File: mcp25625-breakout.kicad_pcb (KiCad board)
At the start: 2 copper layers, 25.4 x 14 mm, 7 parts, among them J1 Conn_01x10, SW1 SW_Slide_with_cover, U1 MCP25625-x-SS, Y1 Resonator

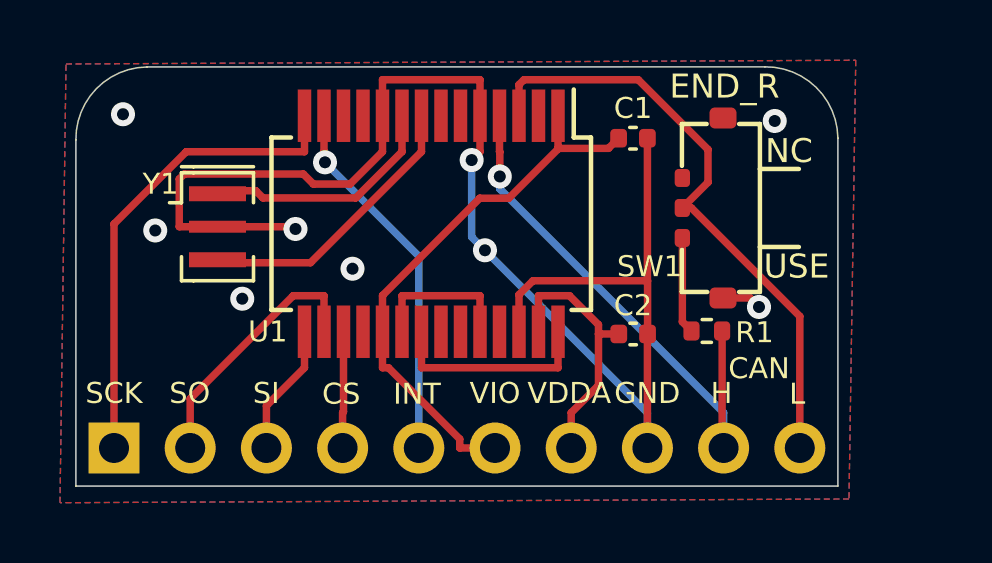
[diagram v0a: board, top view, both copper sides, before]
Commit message: Add reset pad and 16MHz mems as rev2021.07
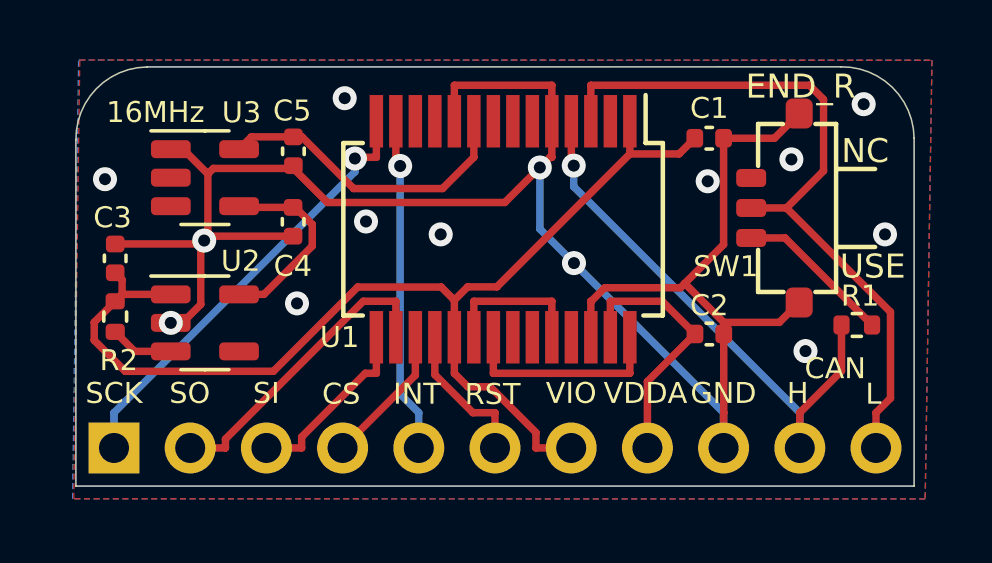
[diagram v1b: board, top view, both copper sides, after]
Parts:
- removed Y1: Resonator, my-kicad-footprints:Resonator_SMD_Murata_CSTxExxV-3Pin_3.0x1.1mm_narrow
- added C3: 0.1uf, Capacitor_SMD:C_0402_1005Metric, F.Cu at (138.0, 77.7)
- added C4: 1uf, Capacitor_SMD:C_0402_1005Metric, F.Cu at (144.0, 76.5)
- added C5: 22pf, Capacitor_SMD:C_0402_1005Metric, F.Cu at (144.0, 74.1)
- added R2: 10k, Resistor_SMD:R_0402_1005Metric, F.Cu at (138.0, 79.6)
- added U2: NJM2866F33, Package_TO_SOT_SMD:SOT-23-5, F.Cu at (141.0, 79.8)
- added U3: SiT2001B-MEMS-Clock-Generator, Package_TO_SOT_SMD:SOT-23-5, F.Cu at (141.0, 75.0)
- J1: value Conn_01x10 -> Conn_01x11; footprint my-kicad-footprints:PinHeader_1x10_P2.54mm_Vertical_witout_silk -> my-kicad-footprints:PinHeader_1x11_P2.54mm_Vertical_witout_silk
- moved R1 5.00 mm to (162.8, 79.9), turned to 0 degrees
- moved C1 2.54 mm to (157.8, 73.7)
- moved C2 2.54 mm to (157.8, 80.2)
- moved SW1 2.54 mm to (160.8, 76.0)
- moved U1 2.40 mm to (151.0, 76.7)
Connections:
- J1 pad 10: /CANL -> /CANH
- J1 pad 6: /V_IO -> /RESET
- J1 pad 7: /V_DDA -> /V_IO
- J1 pad 8: GND -> /V_DDA
- J1 pad 9: /CANH -> GND
- U1 pad 18: Net-(U1-Pad18) -> /RESET
- U1 pad 9: Net-(U1-Pad9) -> /16MHz
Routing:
- net /V_IO: track 18.6 -> 37.1 mm
- net GND: track 50.8 -> 66.1 mm, vias 9 -> 14
- net /16MHz: track 0.00 -> 10.3 mm
- net Net-(U1-Pad8): track 9.53 -> 0.00 mm
- net Net-(U1-Pad9): track 8.09 -> 0.00 mm
- net +3V3: track 0.00 -> 6.52 mm
- net /RESET: track 0.00 -> 4.95 mm
- net /CANL: track 20.5 -> 24.1 mm
- net Net-(R2-Pad2): track 0.00 -> 2.12 mm
- net Net-(R1-Pad2): track 3.23 -> 5.23 mm
- net /SI: track 4.40 -> 6.11 mm
- net /SO: track 8.72 -> 10.3 mm
- net /INT: track 12.4 -> 11.2 mm
- net /SCK: track 16.0 -> 14.9 mm, vias 0 -> 1
- net /CS: track 3.89 -> 4.69 mm
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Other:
- board size 25.4 x 14 mm -> 27.9 x 14 mm
- board text added: "16MHz"
- board text added: "RST"
- board text added: "Reset"
- board text added: "Rev2021.07"
- board text removed: "Rev2021.06"

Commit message: Replace rezonator to crystal
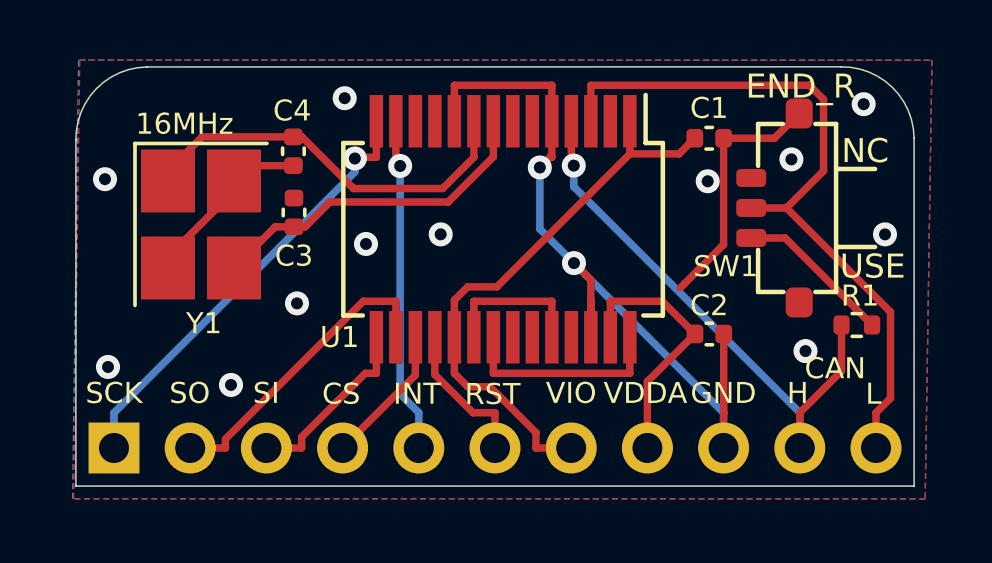
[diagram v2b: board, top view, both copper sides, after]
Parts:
- removed the C4 at (144.0, 76.5)
- removed R2: 10k, Resistor_SMD:R_0402_1005Metric
- removed U2: NJM2866F33, Package_TO_SOT_SMD:SOT-23-5
- removed U3: SiT2001B-MEMS-Clock-Generator, Package_TO_SOT_SMD:SOT-23-5
- added Y1: Crystal_GND24_16MHz, Crystal:Crystal_SMD_SeikoEpson_FA238-4Pin_3.2x2.5mm_HandSoldering, F.Cu at (140.9, 76.5)
- C3: value 0.1uf -> 22pf
- moved C3 6.15 mm to (144.0, 76.2)
- renumbered C5 to C4
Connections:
- net /16MHz renamed Net-(C4-Pad1)
- C3 pad 1: /V_IO -> Net-(C3-Pad1)
- U1 pad 8: Net-(U1-Pad8) -> Net-(C3-Pad1)
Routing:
- net GND: track 66.1 -> 41.4 mm
- net /V_IO: track 37.1 -> 19.0 mm
- net Net-(C3-Pad1): track 0.00 -> 11.4 mm
- net +3V3: track 6.52 -> 0.00 mm
- net Net-(C4-Pad1): track 10.3 -> 13.3 mm
- net Net-(R2-Pad2): track 2.12 -> 0.00 mm
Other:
- board text added: "Rev2021.10"
- board text removed: "Rev2021.07"

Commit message: Apply KiCad6
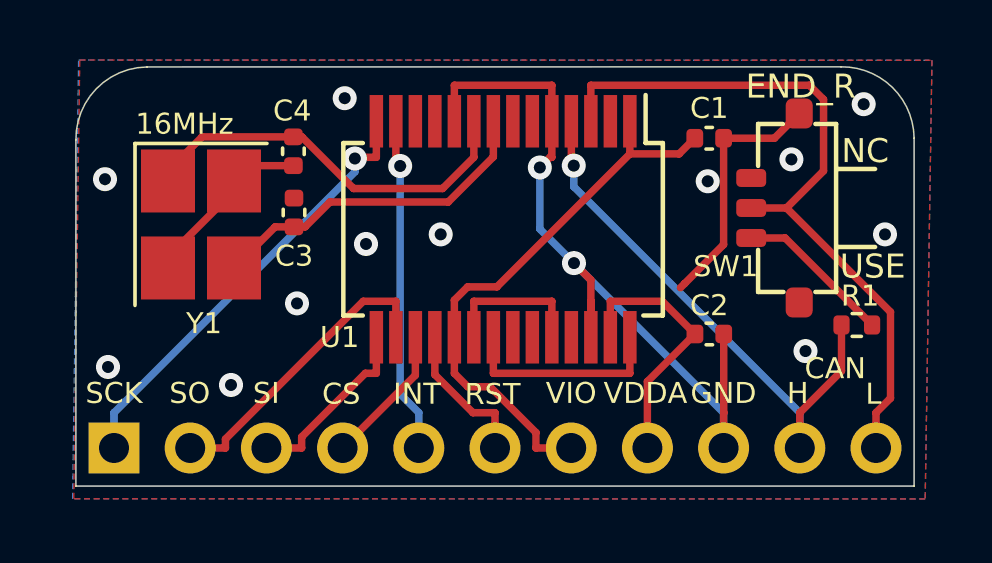
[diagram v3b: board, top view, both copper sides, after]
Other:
- net class Default removed

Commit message: Apply KiCad6 lib
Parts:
- J1: footprint my-kicad-footprints:PinHeader_1x11_P2.54mm_Vertical_witout_silk -> asukiaaa-kicad-footprints:PinHeader_1x11_P2.54mm_Vertical_witout_silk
- SW1: footprint my-kicad-footprints:slide_switch_smd -> asukiaaa-kicad-footprints:slide_switch_smd
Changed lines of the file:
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@@
     )
   )
-  (footprint "my-kicad-footprints:PinHeader_1x11_P2.54mm_Vertical_witout_silk" (layer "F.Cu")
+  (footprint "asukiaaa-kicad-footprints:PinHeader_1x11_P2.54mm_Vertical_witout_silk" (layer "F.Cu")
     (at 138 84 90)
     (descr "Through hole straight pin header, 1x08, 2.54mm pitch, single row")
@@
     )
   )
-  (footprint "my-kicad-footprints:slide_switch_smd" (layer "F.Cu")
+  (footprint "asukiaaa-kicad-footprints:slide_switch_smd" (layer "F.Cu")
     (at 160.84 76 90)
     (descr "https://akizukidenshi.com/download/ds/alps/ssaj120100.pdf")

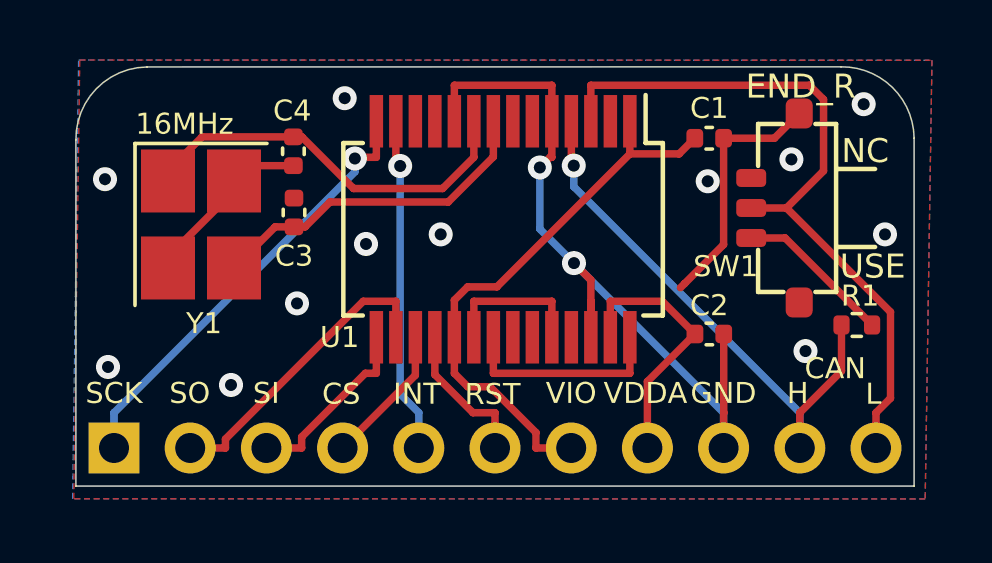
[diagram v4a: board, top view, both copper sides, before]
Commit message: Change to not hand solder pad for crystal
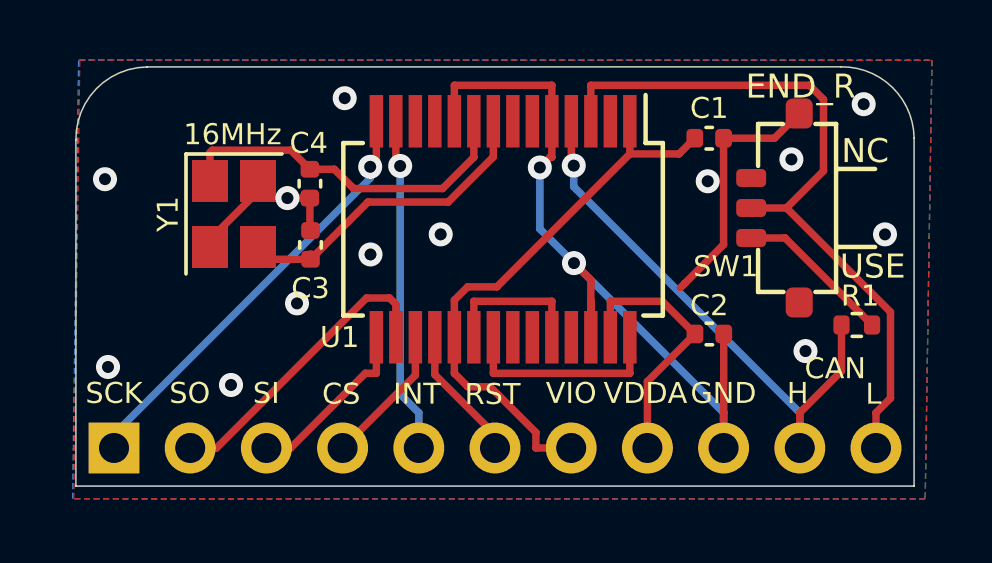
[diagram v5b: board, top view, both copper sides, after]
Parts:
- Y1: footprint Crystal:Crystal_SMD_SeikoEpson_FA238-4Pin_3.2x2.5mm_HandSoldering -> Crystal:Crystal_SMD_SeikoEpson_FA238-4Pin_3.2x2.5mm
- moved C3 1.21 mm to (144.6, 77.2)
- moved C4 1.21 mm to (144.5, 75.2)
- moved Y1 1.15 mm to (142.0, 76.2)
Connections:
- SW1 pad 3: Net-(SW1-Pad3) -> unconnected-(SW1-Pad3)
- U1 pad 11: Net-(U1-Pad11) -> unconnected-(U1-Pad11)
- U1 pad 12: Net-(U1-Pad12) -> unconnected-(U1-Pad12)
- U1 pad 2: Net-(U1-Pad2) -> unconnected-(U1-Pad2)
- U1 pad 22: Net-(U1-Pad22) -> unconnected-(U1-Pad22)
- U1 pad 23: Net-(U1-Pad23) -> unconnected-(U1-Pad23)
- U1 pad 25: Net-(U1-Pad25) -> unconnected-(U1-Pad25)
- U1 pad 6: Net-(U1-Pad6) -> unconnected-(U1-Pad6)
- U1 pad 7: Net-(U1-Pad7) -> unconnected-(U1-Pad7)
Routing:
- net Net-(C4-Pad1): track 13.3 -> 11.9 mm
- net Net-(C3-Pad1): track 11.4 -> 10.6 mm
- net GND: vias 14 -> 15
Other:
- board text added: "Rev2023.02"
- board text removed: "Rev2021.10"

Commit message: Add resistor between rst and vio as rev2023.05
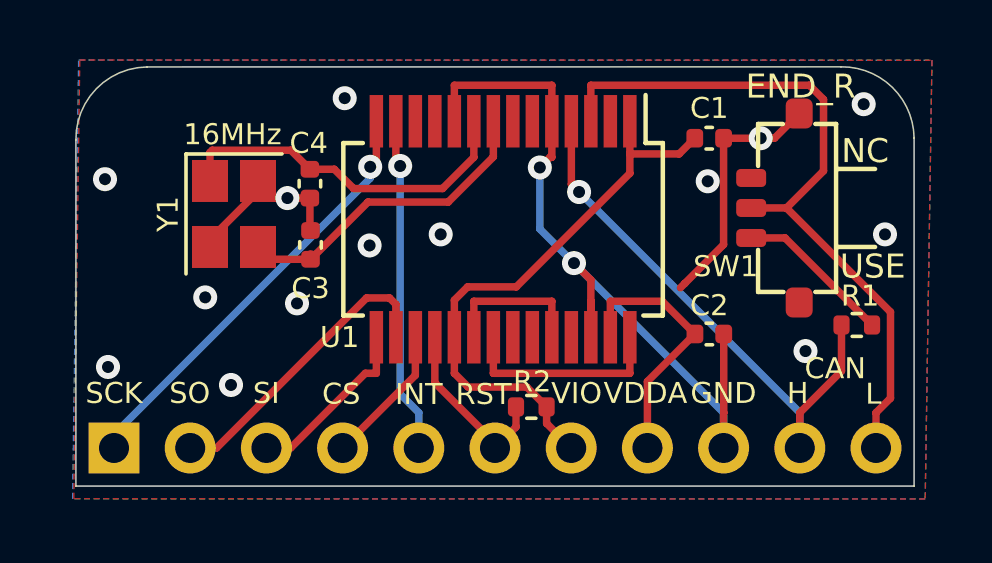
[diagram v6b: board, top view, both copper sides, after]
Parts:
- added R2: 10k, Resistor_SMD:R_0402_1005Metric, F.Cu at (151.9, 82.6)
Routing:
- net /RESET: track 4.52 -> 6.18 mm
- net GND: vias 15 -> 16
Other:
- board text added: "Rev2023.05"
- board text removed: "Rev2023.02"
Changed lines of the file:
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@@
+    )
+  )
+  (footprint "Resistor_SMD:R_0402_1005Metric" (layer "F.Cu")
+    (at 151.91 82.63 180)
+    (descr "Resistor SMD 0402 (1005 Metric), square (rectangular) end terminal, IPC_7351 nominal, (Body size source: IPC-SM-782 page 72, https://www.pcb-3d.com/wordpress/wp-content/uploads/ipc-sm-782a_amendment_1_and_2.pdf), generated with kicad-footprint-generator")
+    (tags "resistor")
+    (property "Sheetfile" "mcp25625-breakout.kicad_sch")
+    (property "Sheetname" "")
+    (attr smd)
+    (fp_text reference "R2" (at -0.03 0.84) (layer "F.SilkS")
+      (effects (font (size 0.7 0.7) (thickness 0.15)))
+    )
+    (fp_text value "10k" (at 0 1.17) (layer "F.Fab")
+      (effects (font (size 1 1) (thickness 0.15)))
+    )
+    (fp_text user "${REFERENCE}" (at 0 0) (layer "F.Fab")
+      (effects (font (size 0.26 0.26) (thickness 0.04)))
+    )
+    (fp_line (start -0.153641 -0.38) (end 0.153641 -0.38) (layer "F.SilkS") (width 0.12))
+    (fp_line (start -0.153641 0.38) (end 0.153641 0.38) (layer "F.SilkS") (width 0.12))
+    (fp_line (start 0.93 0.47) (end -0.93 0.47) (layer "F.CrtYd") (width 0.05))
+    (fp_line (start -0.93 0.47) (end -0.93 -0.47) (layer "F.CrtYd") (width 0.05))
+    (fp_line (start -0.93 -0.47) (end 0.93 -0.47) (layer "F.CrtYd") (width 0.05))
+    (fp_line (start 0.93 -0.47) (end 0.93 0.47) (layer "F.CrtYd") (width 0.05))
+    (fp_line (start 0.525 0.27) (end -0.525 0.27) (layer "F.Fab") (width 0.1))
+    (fp_line (start 0.525 -0.27) (end 0.525 0.27) (layer "F.Fab") (width 0.1))
+    (fp_line (start -0.525 -0.27) (end 0.525 -0.27) (layer "F.Fab") (width 0.1))
+    (fp_line (start -0.525 0.27) (end -0.525 -0.27) (layer "F.Fab") (width 0.1))
+    (pad "1" smd roundrect (at -0.51 0 180) (size 0.54 0.64) (layers "F.Cu" "F.Paste" "F.Mask") (roundrect_rratio 0.25)
+      (net 2 "/V_IO") (pintype "passive"))
+    (pad "2" smd roundrect (at 0.51 0 180) (size 0.54 0.64) (layers "F.Cu" "F.Paste" "F.Mask") (roundrect_rratio 0.25)
+      (net 23 "/RESET") (pintype "passive"))
+    (model "${KICAD6_3DMODEL_DIR}/Resistor_SMD.3dshapes/R_0402_1005Metric.wrl"
+      (offset (xyz 0 0 0))
+      (scale (xyz 1 1 1))
+      (rotate (xyz 0 0 0))
     )
   )
@@
   (gr_line (start 164.67 85.27) (end 164.67 73.67) (layer "Edge.Cuts") (width 0.05))
   (gr_arc (start 136.73 73.73) (mid 137.411731 72.024157) (end 139.1 71.3) (layer "Edge.Cuts") (width 0.05))
-  (gr_text "Rev2023.02" (at 157.265 74.325) (layer "B.SilkS")
+  (gr_text "Rev2023.05" (at 157.265 74.325) (layer "B.SilkS")
     (effects (font (size 1 1) (thickness 0.15)) (justify mirror))
   )
@@
     (effects (font (size 0.8 0.8) (thickness 0.15)))
   )
-  (gr_text "RST" (at 150.62 82.21) (layer "F.SilkS")
+  (gr_text "RST" (at 150.32 82.21) (layer "F.SilkS")
     (effects (font (size 0.7 0.7) (thickness 0.13)))
   )
@@
     (effects (font (size 0.7 0.7) (thickness 0.13)))
   )
-  (gr_text "INT" (at 148.1 82.2) (layer "F.SilkS")
+  (gr_text "INT" (at 148.16 82.21) (layer "F.SilkS")
     (effects (font (size 0.7 0.7) (thickness 0.13)))
   )
@@
     (effects (font (size 0.7 0.7) (thickness 0.13)))
   )
-  (gr_text "VIO" (at 153.24 82.175) (layer "F.SilkS")
+  (gr_text "VIO" (at 153.42 82.18) (layer "F.SilkS")
     (effects (font (size 0.7 0.7) (thickness 0.13)))
   )
@@
   (via (at 137.8 81.3) (size 0.8) (drill 0.4) (layers "F.Cu" "B.Cu") (net 1))
   (via (at 161.05 80.77) (size 0.8) (drill 0.4) (layers "F.Cu" "B.Cu") (net 1))
-  (via (at 146.55 77.55) (size 0.8) (drill 0.4) (layers "F.Cu" "B.Cu") (net 1))
+  (via (at 146.52 77.25) (size 0.8) (drill 0.4) (layers "F.Cu" "B.Cu") (net 1))
   (via (at 152.1945 74.6505) (size 0.8) (drill 0.4) (layers "F.Cu" "B.Cu") (net 1))
-  (via (at 160.58 74.38) (size 0.8) (drill 0.4) (layers "F.Cu" "B.Cu") (net 1))
+  (via (at 141.04 78.98) (size 0.8) (drill 0.4) (layers "F.Cu" "B.Cu") (free) (net 1))
+  (via (at 159.555 73.675) (size 0.8) (drill 0.4) (layers "F.Cu" "B.Cu") (net 1))
   (via (at 137.7 75.04) (size 0.8) (drill 0.4) (layers "F.Cu" "B.Cu") (net 1))
   (segment (start 153.33265 77.83735) (end 152.1945 76.6992) (width 0.25) (layer "B.Cu") (net 1))
@@
   (segment (start 158.32 84) (end 158.32 82.8247) (width 0.25) (layer "B.Cu") (net 1))
   (segment (start 152.1945 76.6992) (end 152.1945 74.6505) (width 0.25) (layer "B.Cu") (net 1))
-  (segment (start 149.345 79.0724) (end 149.345 80.31) (width 0.25) (layer "F.Cu") (net 2))
+  (segment (start 149.345 79.0724) (end 149.7884 78.629) (width 0.25) (layer "F.Cu") (net 2))
+  (segment (start 149.8047 81.97) (end 151.76 81.97) (width 0.25) (layer "F.Cu") (net 2))
+  (segment (start 149.7884 78.629) (end 151.411 78.629) (width 0.25) (layer "F.Cu") (net 2))
   (segment (start 156.8371 74.1979) (end 155.195 74.1979) (width 0.25) (layer "F.Cu") (net 2))
   (segment (start 157.36 73.675) (end 156.8371 74.1979) (width 0.25) (layer "F.Cu") (net 2))
-  (segment (start 149.345 81.5103) (end 149.7954 81.9607) (width 0.25) (layer "F.Cu") (net 2))
-  (segment (start 149.7884 78.629) (end 150.7639 78.629) (width 0.25) (layer "F.Cu") (net 2))
-  (segment (start 149.7954 81.9607) (end 150.5396 81.9607) (width 0.25) (layer "F.Cu") (net 2))
-  (segment (start 152.0647 83.4858) (end 152.0647 84) (width 0.25) (layer "F.Cu") (net 2))
-  (segment (start 153.24 84) (end 152.0647 84) (width 0.25) (layer "F.Cu") (net 2))
+  (segment (start 155.195 74.845) (end 155.195 74.1979) (width 0.25) (layer "F.Cu") (net 2))
+  (segment (start 152.42 83.18) (end 153.24 84) (width 0.25) (layer "F.Cu") (net 2))
+  (segment (start 151.411 78.629) (end 155.195 74.845) (width 0.25) (layer "F.Cu") (net 2))
   (segment (start 149.345 80.31) (end 149.345 81.5103) (width 0.25) (layer "F.Cu") (net 2))
-  (segment (start 150.5396 81.9607) (end 152.0647 83.4858) (width 0.25) (layer "F.Cu") (net 2))
   (segment (start 155.195 73.11) (end 155.195 74.1979) (width 0.25) (layer "F.Cu") (net 2))
-  (segment (start 150.7639 78.629) (end 155.195 74.1979) (width 0.25) (layer "F.Cu") (net 2))
-  (segment (start 149.345 79.0724) (end 149.7884 78.629) (width 0.25) (layer "F.Cu") (net 2))
+  (segment (start 149.345 80.31) (end 149.345 79.0724) (width 0.25) (layer "F.Cu") (net 2))
+  (segment (start 151.76 81.97) (end 152.42 82.63) (width 0.25) (layer "F.Cu") (net 2))
+  (segment (start 149.345 81.5103) (end 149.8047 81.97) (width 0.25) (layer "F.Cu") (net 2))
+  (segment (start 152.42 82.63) (end 152.42 83.18) (width 0.25) (layer "F.Cu") (net 2))
   (segment (start 156.2747 79.1097) (end 157.365 80.2) (width 0.25) (layer "F.Cu") (net 3))
   (segment (start 157.365 80.2) (end 155.78 81.785) (width 0.25) (layer "F.Cu") (net 3))
@@
   (segment (start 160.4167 76) (end 159.24 76) (width 0.25) (layer "F.Cu") (net 4))
   (segment (start 160.86 84) (end 160.86 82.8247) (width 0.25) (layer "F.Cu") (net 5))
-  (segment (start 153.245 74.5076) (end 153.245 73.11) (width 0.25) (layer "F.Cu") (net 5))
-  (segment (start 153.3255 74.5881) (end 153.245 74.5076) (width 0.25) (layer "F.Cu") (net 5))
+  (segment (start 153.245 75.2097) (end 153.245 73.11) (width 0.25) (layer "F.Cu") (net 5))
   (segment (start 162.25 81.4347) (end 160.86 82.8247) (width 0.25) (layer "F.Cu") (net 5))
   (segment (start 162.25 79.9) (end 162.25 81.4347) (width 0.25) (layer "F.Cu") (net 5))
-  (via (at 153.3255 74.5881) (size 0.8) (drill 0.4) (layers "F.Cu" "B.Cu") (net 5))
-  (segment (start 160.86 84) (end 160.86 82.8247) (width 0.25) (layer "B.Cu") (net 5))
-  (segment (start 160.86 82.8247) (end 153.3255 75.2902) (width 0.25) (layer "B.Cu") (net 5))
-  (segment (start 153.3255 75.2902) (end 153.3255 74.5881) (width 0.25) (layer "B.Cu") (net 5))
+  (segment (start 153.50265 75.46735) (end 153.245 75.2097) (width 0.25) (layer "F.Cu") (net 5))
+  (via (at 153.50265 75.46735) (size 0.8) (drill 0.4) (layers "F.Cu" "B.Cu") (net 5))
+  (segment (start 160.86 82.8247) (end 160.86 84) (width 0.25) (layer "B.Cu") (net 5))
+  (segment (start 153.50265 75.46735) (end 160.86 82.8247) (width 0.25) (layer "B.Cu") (net 5))
   (segment (start 147.395 74.4564) (end 147.539 74.6004) (width 0.25) (layer "F.Cu") (net 6))
   (segment (start 147.395 73.11) (end 147.395 74.4564) (width 0.25) (layer "F.Cu") (net 6))
@@
   (segment (start 160.37 77) (end 159.24 77) (width 0.25) (layer "F.Cu") (net 21))
   (segment (start 163.27 79.9) (end 160.37 77) (width 0.25) (layer "F.Cu") (net 21))
-  (segment (start 150.7 84) (end 150.7 83.5593) (width 0.25) (layer "F.Cu") (net 23))
-  (segment (start 150.7 83.5593) (end 148.695 81.5543) (width 0.25) (layer "F.Cu") (net 23))
-  (segment (start 148.695 81.5543) (end 148.695 80.31) (width 0.25) (layer "F.Cu") (net 23))
+  (segment (start 150.7 84) (end 150.7 83.83) (width 0.25) (layer "F.Cu") (net 23))
+  (segment (start 148.695 81.825) (end 148.695 80.31) (width 0.25) (layer "F.Cu") (net 23))
+  (segment (start 150.7 83.83) (end 148.695 81.825) (width 0.25) (layer "F.Cu") (net 23))
+  (segment (start 151.4 83.3) (end 150.7 84) (width 0.25) (layer "F.Cu") (net 23))
+  (segment (start 151.4 82.63) (end 151.4 83.3) (width 0.25) (layer "F.Cu") (net 23))
   (segment (start 150.645 74.29671) (end 150.645 73.11) (width 0.25) (layer "F.Cu") (net 24))
   (segment (start 144.55 77.71) (end 143.21 77.71) (width 0.25) (layer "F.Cu") (net 24))
